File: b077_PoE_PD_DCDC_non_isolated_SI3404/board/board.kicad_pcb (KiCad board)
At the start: 2 copper layers, 45 x 29 mm, 27 parts, among them J1 013_PoE_rectified, J2 003_power, U1 Si3404

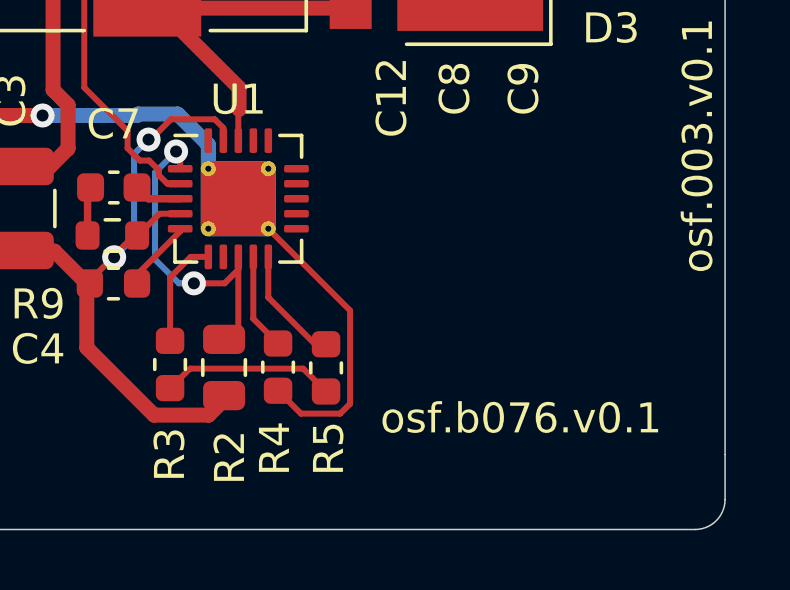
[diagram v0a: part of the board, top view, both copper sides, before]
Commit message: fixed missing connections mentioned in PR #64. cleaned up lib connections and bumped version to 1.0
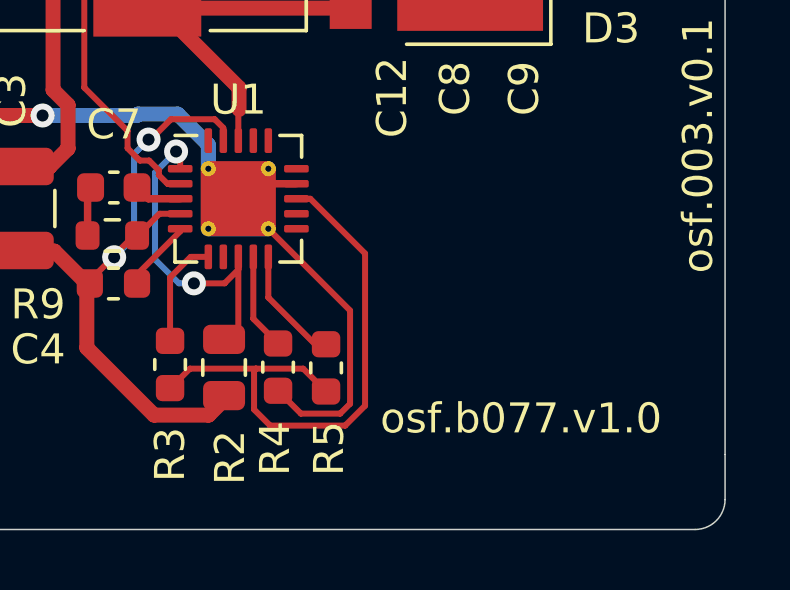
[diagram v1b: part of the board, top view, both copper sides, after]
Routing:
- net Net-(R3-Pad2): track 5.79 -> 19.5 mm
- net Net-(C1-Pad2): track 42.9 -> 45.0 mm
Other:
- board text added: "osf.b077.v1.0"
- board text removed: "osf.b076.v0.1"
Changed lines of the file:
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@@
   (gr_arc (start 174.999999 111.999999) (mid 174.707106 112.707106) (end 173.999999 112.999999) (layer "Edge.Cuts") (width 0.05))
   (gr_arc (start 131 113) (mid 130.292893 112.707107) (end 130 112) (layer "Edge.Cuts") (width 0.05))
-  (gr_text "osf.b076.v0.1" (at 168.2 109.3) (layer "F.SilkS")
+  (gr_text "osf.b077.v1.0" (at 168.2 109.3) (layer "F.SilkS")
     (effects (font (size 1 1) (thickness 0.15)))
   )
@@
   (segment (start 143.4 97.9) (end 143.4 91) (width 0.5) (layer "F.Cu") (net 3))
   (segment (start 144.7 99.2) (end 143.4 97.9) (width 0.5) (layer "F.Cu") (net 3))
+  (segment (start 159.275 101.475) (end 158.775 101.975) (width 0.25) (layer "F.Cu") (net 3))
   (segment (start 143.4 91) (end 138.75 86.35) (width 0.5) (layer "F.Cu") (net 3))
   (segment (start 137.65 86.35) (end 136 88) (width 0.5) (layer "F.Cu") (net 3))
+  (segment (start 160.7125 101.475) (end 159.275 101.475) (width 0.25) (layer "F.Cu") (net 3))
   (segment (start 152.2505 99.2) (end 144.7 99.2) (width 0.5) (layer "F.Cu") (net 3))
   (segment (start 138.75 86.35) (end 137.65 86.35) (width 0.5) (layer "F.Cu") (net 3))
@@
   (segment (start 157.775 103.9125) (end 157.1875 103.9125) (width 0.2) (layer "F.Cu") (net 22))
   (segment (start 157.16202 107.63798) (end 156.5 108.3) (width 0.2) (layer "F.Cu") (net 23))
-  (segment (start 160.93798 107.63798) (end 157.16202 107.63798) (width 0.2) (layer "F.Cu") (net 23))
+  (segment (start 159.836059 109.536539) (end 162.336411 109.536539) (width 0.2) (layer "F.Cu") (net 23))
+  (segment (start 161.175 101.975) (end 160.7125 101.975) (width 0.2) (layer "F.Cu") (net 23))
+  (segment (start 159.36202 107.63798) (end 159.29952 107.70048) (width 0.2) (layer "F.Cu") (net 23))
+  (segment (start 162.336411 109.536539) (end 163 108.87295) (width 0.2) (layer "F.Cu") (net 23))
+  (segment (start 159.29952 109) (end 159.836059 109.536539) (width 0.2) (layer "F.Cu") (net 23))
   (segment (start 161.7 108.4) (end 160.93798 107.63798) (width 0.2) (layer "F.Cu") (net 23))
+  (segment (start 159.29952 107.70048) (end 159.29952 109) (width 0.2) (layer "F.Cu") (net 23))
+  (segment (start 163 103.8) (end 161.175 101.975) (width 0.2) (layer "F.Cu") (net 23))
+  (segment (start 159.36202 107.63798) (end 157.16202 107.63798) (width 0.2) (layer "F.Cu") (net 23))
+  (segment (start 160.93798 107.63798) (end 159.36202 107.63798) (width 0.2) (layer "F.Cu") (net 23))
+  (segment (start 163 108.87295) (end 163 103.8) (width 0.2) (layer "F.Cu") (net 23))
   (segment (start 159.275 103.9125) (end 159.275 105.975) (width 0.2) (layer "F.Cu") (net 24))
   (segment (start 159.275 105.975) (end 160.1 106.8) (width 0.2) (layer "F.Cu") (net 24))

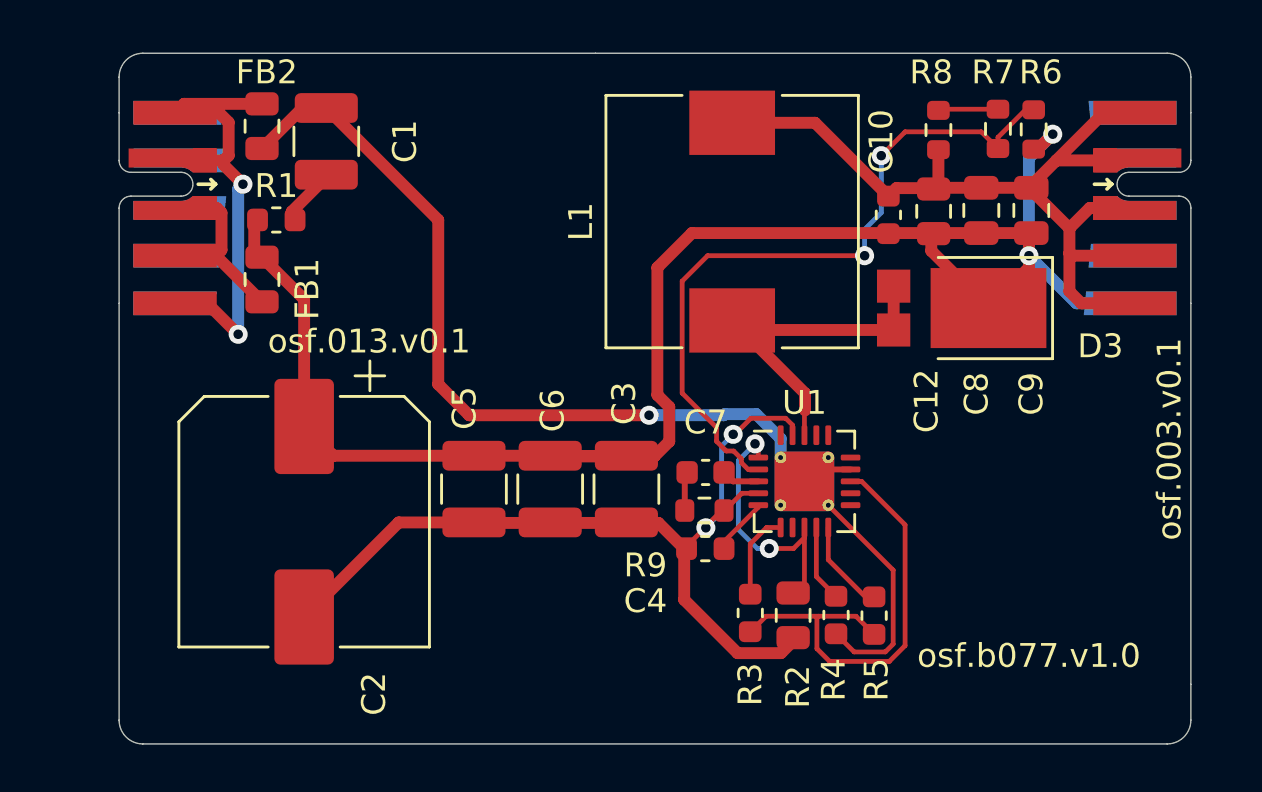
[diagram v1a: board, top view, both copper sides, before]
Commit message: Fix supply, better thermal mgmt.
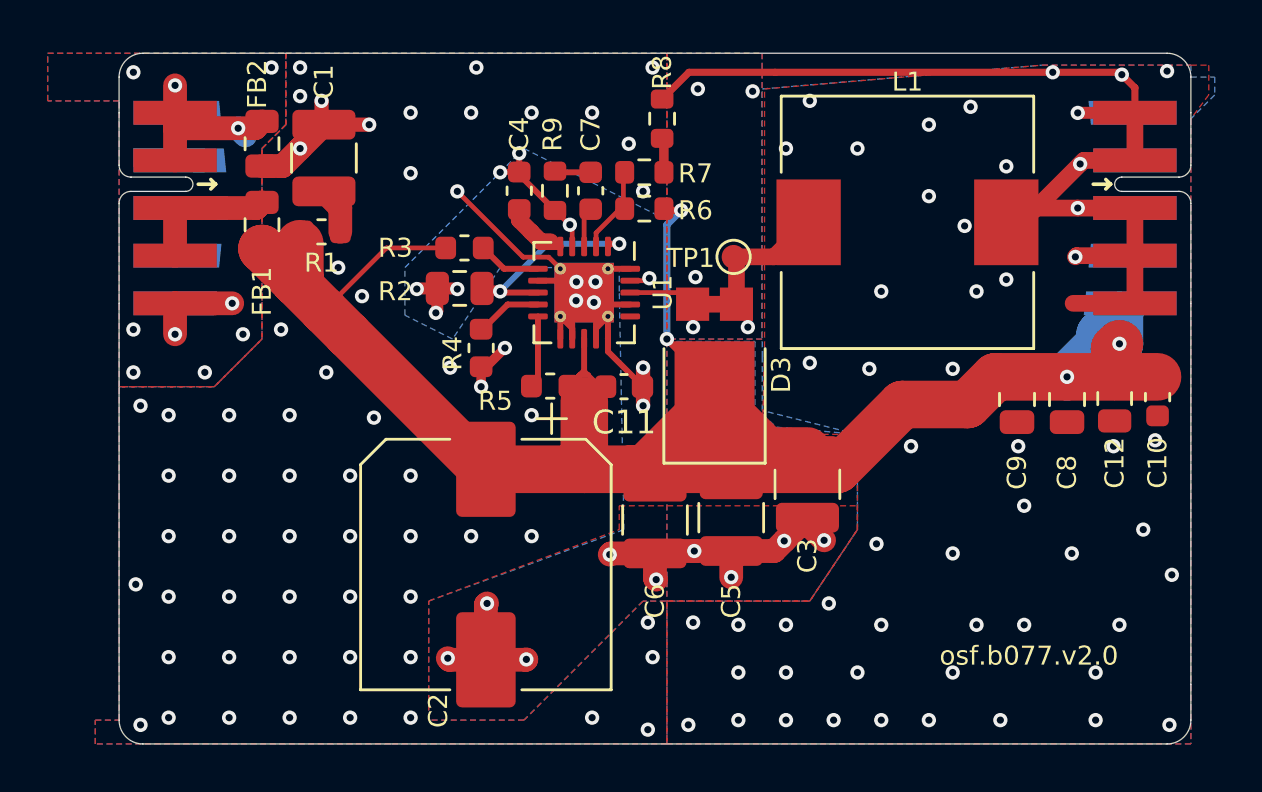
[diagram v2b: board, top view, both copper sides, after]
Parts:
- added C11: 100nF, Capacitor_SMD:C_0603_1608Metric, F.Cu at (151.2, 98.0)
- added TP1: GND2_OUT, TestPoint:TestPoint_Pad_D1.0mm, F.Cu at (155.8, 92.5)
- moved R2 19.6 mm to (144.3, 93.9), turned to 0 degrees
- moved R3 19.5 mm to (144.5, 92.2), turned to 180 degrees
- moved R4 18.6 mm to (145.2, 96.4)
- moved C4 16.9 mm to (146.8, 89.8), turned to -90 degrees
- moved R6 16.7 mm to (152.1, 90.5), turned to 180 degrees
- moved R5 16.7 mm to (148.1, 98.0), turned to 0 degrees
- moved R7 15.0 mm to (152.1, 89.0), turned to 0 degrees
- moved R9 14.8 mm to (148.3, 89.8), turned to -90 degrees
- moved C10 13.6 mm to (173.6, 98.4), turned to -90 degrees
- moved C7 12.8 mm to (149.8, 89.8), turned to 90 degrees
- moved U1 12.2 mm to (149.5, 94.0), turned to -90 degrees
- moved R8 11.6 mm to (152.8, 86.8), turned to 90 degrees
- moved C12 10.9 mm to (171.8, 98.5), turned to -90 degrees
- moved C5 10.9 mm to (155.7, 103.5)
- moved D3 10.7 mm to (155.0, 97.4), turned to 90 degrees
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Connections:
- net Net-(D3-Pad2) renamed /dcdc/GND2_OUT
- net VDD renamed /dcdc/VDD
- net VSS renamed /dcdc/VSS
- C1 pad 2: Net-(C1-Pad2) -> /dcdc/GND_IN
- C10 pad 1: /dcdc/5V -> /dcdc/VPOS
- C12 pad 1: /dcdc/5V -> /dcdc/VPOS
- C2 pad 1: /dcdc/5V -> /dcdc/VPOS
- C3 pad 1: /dcdc/5V -> /dcdc/VPOS
- C5 pad 1: /dcdc/5V -> /dcdc/VPOS
- C6 pad 1: /dcdc/5V -> /dcdc/VPOS
- C8 pad 1: /dcdc/5V -> /dcdc/VPOS
- C9 pad 1: /dcdc/5V -> /dcdc/VPOS
- D3 pad 1: /dcdc/5V -> /dcdc/VPOS
- FB1 pad 2: /dcdc/5V -> /dcdc/VPOS
- FB2 pad 2: Net-(C1-Pad2) -> /dcdc/GND_IN
- J2 pad 10: /dcdc/5V -> /dcdc/VPOS
- R1 pad 1: /dcdc/5V -> /dcdc/VPOS
- R3 pad 2: Net-(R3-Pad2) -> /dcdc/VPOS
- R4 pad 1: Net-(C1-Pad2) -> /dcdc/GND_IN
- R5 pad 2: Net-(R3-Pad2) -> /dcdc/VPOS
- R6 pad 1: /dcdc/5V -> /dcdc/VPOS
- U1 pad 11: unconnected-(U1-Pad11) -> /dcdc/GND_IN
- U1 pad 12: unconnected-(U1-Pad12) -> /dcdc/GND_IN
- U1 pad 13: Net-(R3-Pad2) -> /dcdc/VPOS
- U1 pad 14: Net-(C1-Pad2) -> /dcdc/GND_IN
- U1 pad 15: unconnected-(U1-Pad15) -> /dcdc/GND_IN
- U1 pad 17: unconnected-(U1-Pad17) -> /dcdc/GND_IN
- U1 pad 20: unconnected-(U1-Pad20) -> /dcdc/GND_IN
- U1 pad 21: Net-(C1-Pad2) -> /dcdc/GND_IN
- U1 pad 7: unconnected-(U1-Pad7) -> /dcdc/GND_IN
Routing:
- net /dcdc/VPOS: track 0.00 -> 86.2 mm, vias 0 -> 4
- net /dcdc/5V: track 72.3 -> 0.00 mm, vias 2 -> 0
- net Net-(C1-Pad2): track 45.0 -> 0.00 mm, vias 1 -> 0
- net /dcdc/GND_IN: track 0.00 -> 29.9 mm, vias 0 -> 67
- net /dcdc/FBH: track 30.3 -> 3.70 mm, vias 2 -> 0
- net Net-(R3-Pad2): track 19.5 -> 0.00 mm
- net /dcdc/GND2: track 36.1 -> 47.3 mm, vias 0 -> 53
- net /dcdc/VSS: track 37.8 -> 27.4 mm, vias 2 -> 16
- net GND: track 19.6 -> 11.0 mm, vias 2 -> 10
- net /dcdc/GND2_OUT: track 14.9 -> 10.4 mm, vias 0 -> 5
- net Net-(R2-Pad2): track 11.3 -> 9.59 mm
- net /dcdc/48V: track 7.13 -> 5.75 mm
- net Net-(R7-Pad2): track 2.52 -> 1.46 mm
- net Net-(R3-Pad1): track 3.68 -> 2.66 mm
- net Net-(R5-Pad1): track 3.92 -> 3.04 mm
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- added copper zone on B.Cu, net /dcdc/GND2
- added copper zone on F.Cu, net /dcdc/GND2
- added copper zone on B.Cu, net /dcdc/GND2_OUT
- added copper zone on F.Cu, net /dcdc/GND2_OUT
- added copper zone on B.Cu, net /dcdc/GND_IN
- added copper zone on F.Cu, net /dcdc/GND_IN
- added copper zone on B.Cu, net /dcdc/VSS
- added copper zone on F.Cu, net /dcdc/VSS
- added copper zone on B.Cu, net GND
- added copper zone on F.Cu, net GND
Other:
- board text added: "osf.b077.v2.0"
- board text removed: "osf.003.v0.1"
- board text removed: "osf.013.v0.1"
- board text removed: "osf.b077.v1.0"

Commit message: Update Silk
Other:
- board text added: "osf.b077.v0.3"
- board text removed: "osf.b077.v2.0"
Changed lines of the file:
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@@
   (gr_arc (start 174.999999 111.999999) (mid 174.707106 112.707106) (end 173.999999 112.999999) (layer "Edge.Cuts") (width 0.05))
   (gr_arc (start 131 113) (mid 130.292893 112.707107) (end 130 112) (layer "Edge.Cuts") (width 0.05))
-  (gr_text "osf.b077.v2.0" (at 168.2 109.3) (layer "F.SilkS")
+  (gr_text "osf.b077.v0.3" (at 168.2 109.3) (layer "F.SilkS")
     (effects (font (size 0.8 0.8) (thickness 0.127)))
   )
